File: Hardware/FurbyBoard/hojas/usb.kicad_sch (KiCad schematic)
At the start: 9 parts, among them J1 USB-C 16P, U1 USBLC6-2SC6

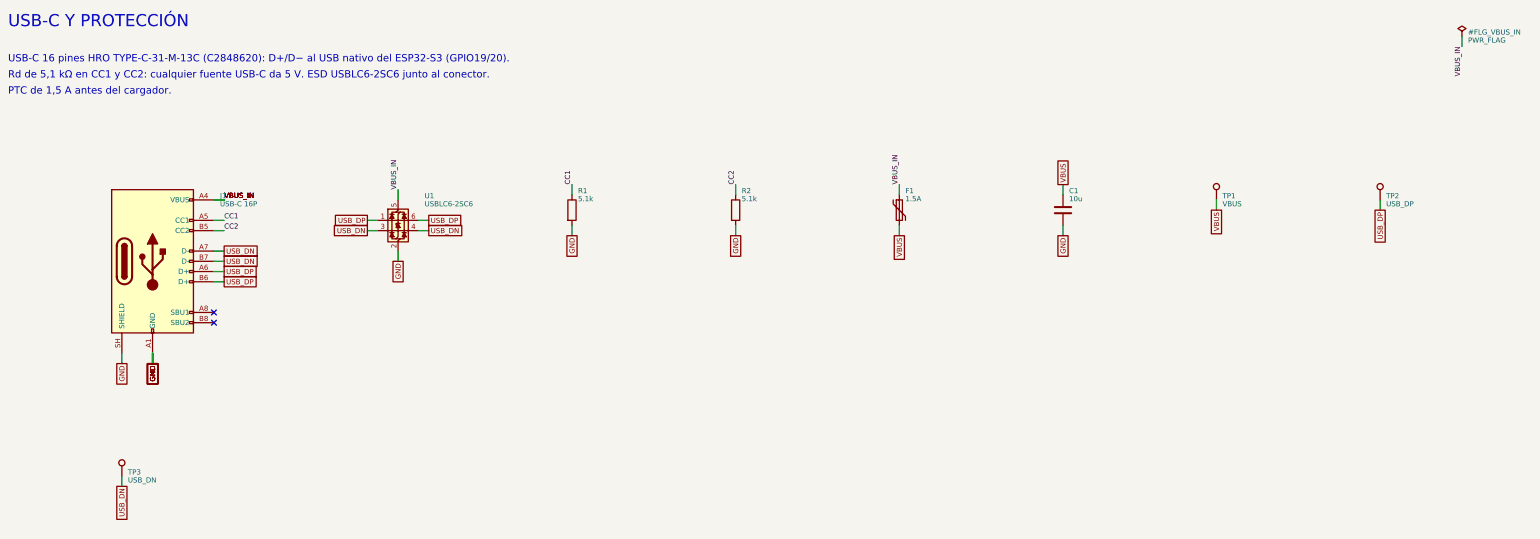
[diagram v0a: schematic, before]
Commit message: Refactor: pads de cable agrupados por zona y etiquetas globales
- Motor en J9 con leva, encoder y sensores; altavoz en J8 con inclinación y
  lengua; luz en J7 con el IR. Desaparecen J4 y J10: cada grupo sale por el
  borde más cercano a su destino.
- Micro en 2x03 en vez de 1x06 para que quepa junto al borde derecho.
- Todas las etiquetas del esquemático son globales, así el nombre de red
  coincide con el del PCB (paridad sin prefijos de hoja).
- ERC 0 errores, 0 avisos.

Co-Authored-By: Claude Opus 5.5 (1M context) <noreply@anthropic.com>
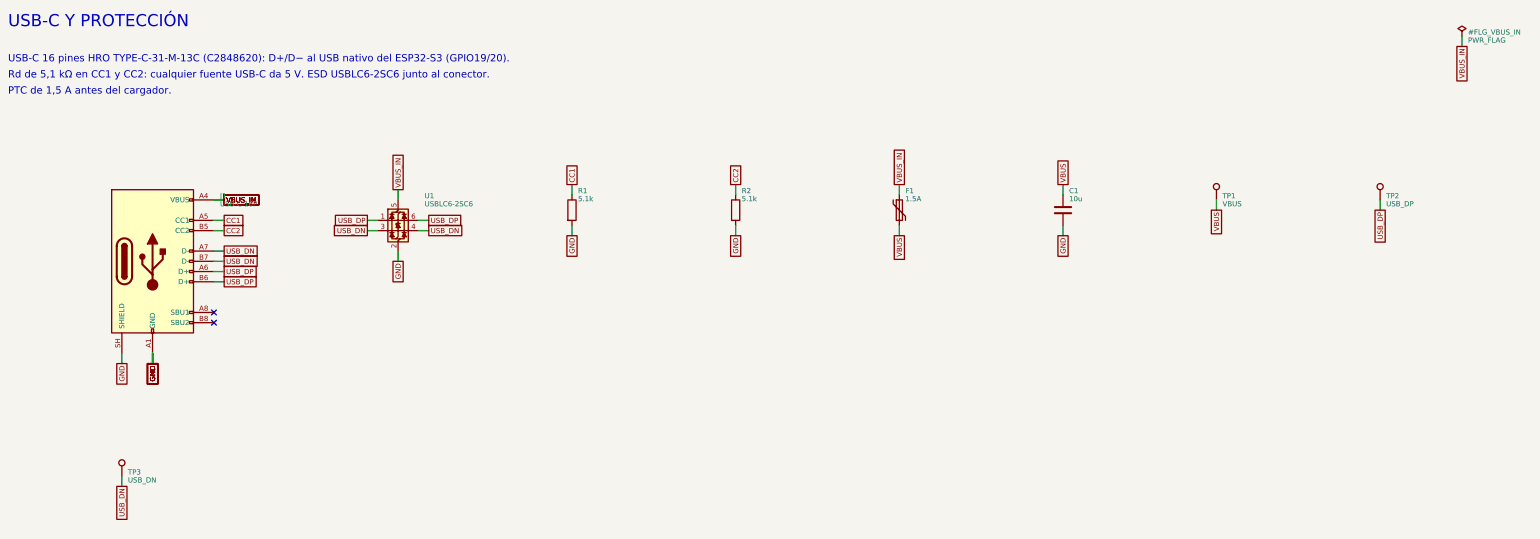
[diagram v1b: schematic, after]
